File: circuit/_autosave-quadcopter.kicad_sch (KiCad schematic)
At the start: 79 parts, among them J1 Conn_01x01_Female, J10 Conn_01x01_Female, J11 Conn_01x01_Female, J12 Conn_01x01_Female, J13 Conn_01x01_Female, J14 Conn_01x01_Female, J15 Conn_01x01_Female, J16 Conn_01x01_Female, J17 Conn_01x01_Female, J18 USB_C_Receptacle_USB2.0, J19 Conn_01x08_Male, J2 Conn_01x01_Female, J20 Conn_01x04_Male, J21 Conn_01x01_Female, J22 Conn_01x01_Female, J23 Conn_01x01_Female, J24 Conn_01x01_Female, J25 Conn_01x01_Female, J26 Conn_01x01_Female, J27 Conn_01x01_Female, J28 Conn_01x01_Female, J29 Conn_01x01_Female, J3 Conn_01x01_Female, J30 Conn_01x01_Female, J31 Conn_01x01_Female, J32 Conn_01x01_Female, J33 Conn_01x01_Female, J36 Conn_01x01_Female, J37 Conn_01x01_Female, J38 Conn_01x01_Female, J39 Conn_01x01_Female, J4 Conn_01x01_Female, J40 Conn_01x01_Female, J41 Conn_01x01_Female, J42 Conn_01x01_Female, J43 Conn_01x01_Female, J44 Conn_01x01_Female, J45 Conn_01x01_Female, J46 Conn_01x01_Female, J47 Conn_01x01_Female, J48 Conn_01x01_Female, J49 Conn_01x01_Female, J5 Conn_01x01_Female, J50 Conn_01x01_Female, J6 Conn_01x01_Female, J7 Conn_01x01_Female, J8 Conn_01x01_Female, J9 Conn_01x01_Female, SW1 SW_Push_Dual, U1 STM32G431CBU6, U2 ICM-42605, U3 DPS310, U4 3V3, U5 5V, Y1 16M

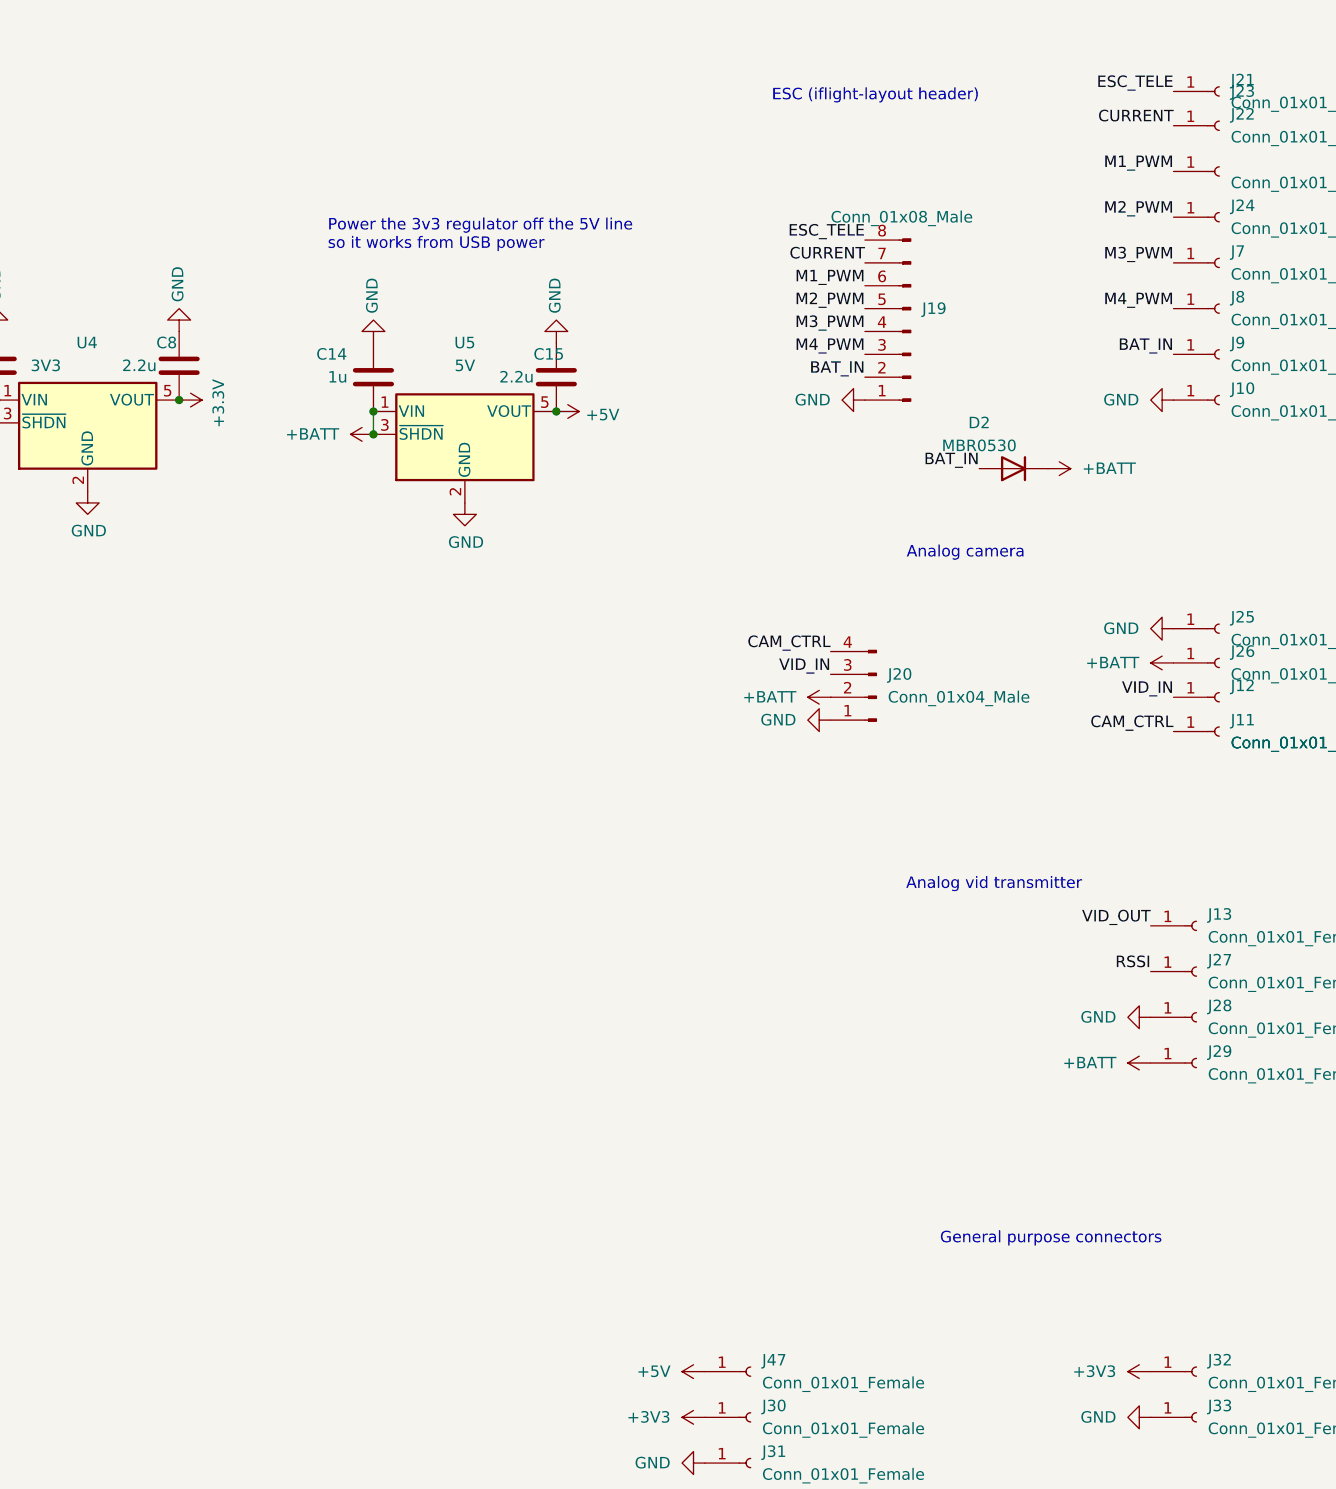
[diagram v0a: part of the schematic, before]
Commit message: Attempting to make the board compatible with 20mm frames
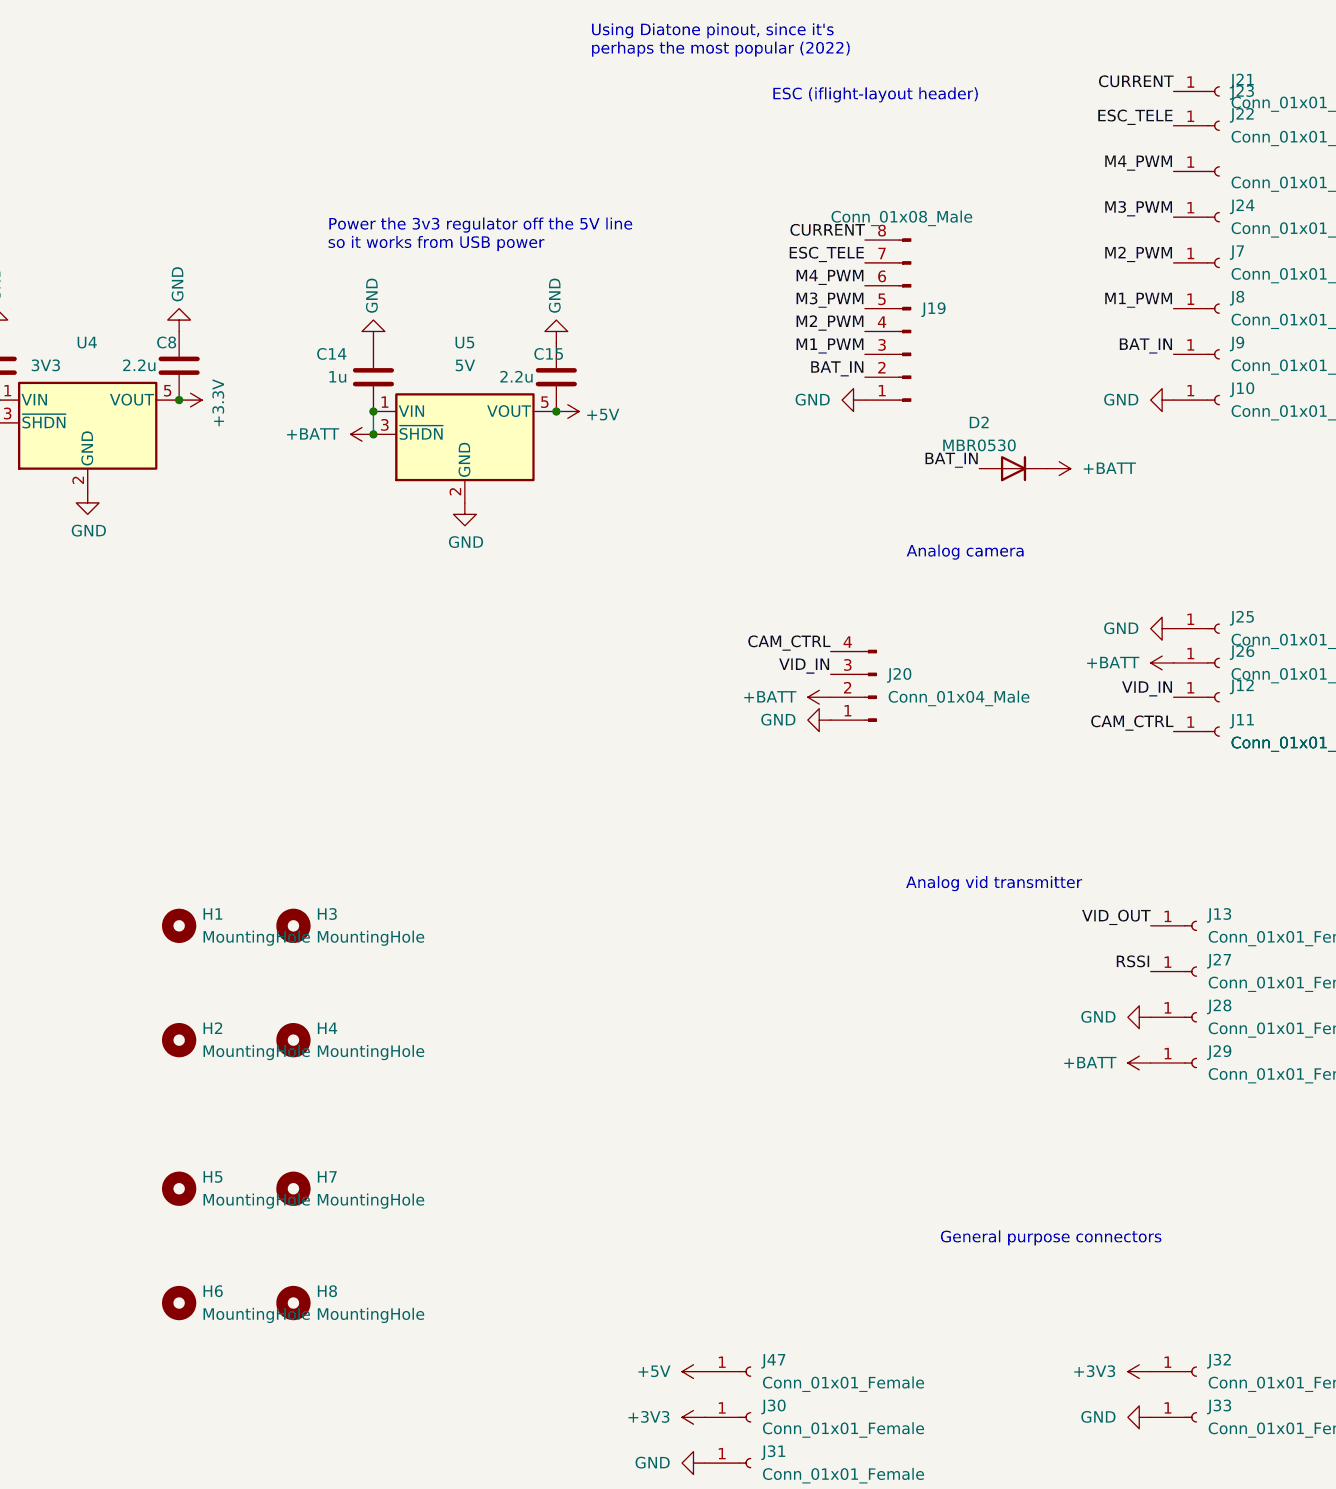
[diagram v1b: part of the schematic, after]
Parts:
- added H1, H2, H3, H4: MountingHole, MountingHole:MountingHole_3.2mm_M3, symbol Mechanical:MountingHole
- added H5, H6, H7, H8: MountingHole, MountingHole:MountingHole_2.2mm_M2, symbol Mechanical:MountingHole
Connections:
- net CURRENT: now also J19.8 (Pin_8), J21.1 (Pin_1); no longer J19.7 (Pin_7), J22.1 (Pin_1)
- net ESC_TELE: now also J19.7 (Pin_7), J22.1 (Pin_1); no longer J19.8 (Pin_8), J21.1 (Pin_1)
- net M1_PWM: now also J19.3 (Pin_3), J8.1 (Pin_1); no longer J19.6 (Pin_6), J23.1 (Pin_1)
- net M2_PWM: now also J19.4 (Pin_4), J7.1 (Pin_1); no longer J19.5 (Pin_5), J24.1 (Pin_1)
- net M3_PWM: now also J19.5 (Pin_5), J24.1 (Pin_1); no longer J19.4 (Pin_4), J7.1 (Pin_1)
- net M4_PWM: now also J19.6 (Pin_6), J23.1 (Pin_1); no longer J19.3 (Pin_3), J8.1 (Pin_1)
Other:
- note added: "Using Diatone pinout, since it's perhaps the most popular (2022)"

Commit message: More work on PCB
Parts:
- added C16, C17: 100n, Capacitor_SMD:C_0402_1005Metric, symbol Device:C
- H5, H6, H7, H8: footprint MountingHole:MountingHole_2.2mm_M2 -> MountingHole:MountingHole_3.2mm_M3
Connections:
- net +3V3: now also C10.2, C11.2, C12.2, C13.2, U1.1 (VBAT), U1.20 (VREF+), U1.21 (VDDA), U1.23 (VDD), U1.35 (VDD), U1.48 (VDD), C16.2, C17.2
- net GND: now also C10.1, C11.1, C12.1, C13.1, U1.49 (EP-GND), C16.1, C17.1
- net at U1.5 (PF0-OSC_IN): now also C6.2, Y1.1
- net at U1.6 (PF1-OSC_OUT): now also C9.2, Y1.3
- now unconnected: U1.8 (PF0-OSC_IN), U1.9 (PF1-OSC_OUT)
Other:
- moved on the sheet: C10, C11, C12, C13

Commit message: More work on PCB
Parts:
- removed SW1: SW_Push_Dual, Button_Switch_THT:SW_PUSH_6mm_H9.5mm, symbol Switch:SW_Push_Dual
- added SW1: SW_DIP_x01, Anyleaf_Shared:SW-SMD-2_3.6x6.0x8.0, symbol Switch:SW_DIP_x01
- J11, J12, J25, J26: footprint TestPoint:TestPoint_Pad_2.0x2.0mm -> TestPoint:TestPoint_Pad_1.5x1.5mm
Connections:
- net SCK_I2C_2 is gone; now on net SCL2: U3.4 (SCK)
- net SDA_2 is gone; now on net SDA2: U3.3 (SDI)
- net +3V3: now also R6.2; no longer R6.1
- net BOOT0: now also R1.2, U1.46 (PB8-BOOT0), SW1.1
- net GND: now also R1.1; no longer R1.2
- net SCL1: now also J15.1 (Pin_1); no longer J5.1 (Pin_1)
- net SCL3: now also J5.1 (Pin_1); no longer J15.1 (Pin_1)
- net SDA1: now also J46.1 (Pin_1); no longer J6.1 (Pin_1)
- net SDA3: now also J6.1 (Pin_1); no longer J46.1 (Pin_1)
- net UART1_RX: now also J45.1 (Pin_1); no longer J37.1 (Pin_1)
- net UART1_TX: now also J44.1 (Pin_1); no longer J36.1 (Pin_1)
- net UART2_RX: now also J43.1 (Pin_1); no longer J39.1 (Pin_1)
- net UART2_TX: now also J42.1 (Pin_1); no longer J38.1 (Pin_1)
- net UART4_RX: now also J39.1 (Pin_1); no longer J43.1 (Pin_1)
- net UART4_TX: now also J38.1 (Pin_1); no longer J42.1 (Pin_1)
- net UART5_RX: now also J37.1 (Pin_1); no longer J45.1 (Pin_1)
- net UART5_TX: now also J36.1 (Pin_1); no longer J44.1 (Pin_1)
- new net: R6.1, SW1.2
- no-connect marks 2 -> 1
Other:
- moved on the sheet: J30, J48, R1, R6

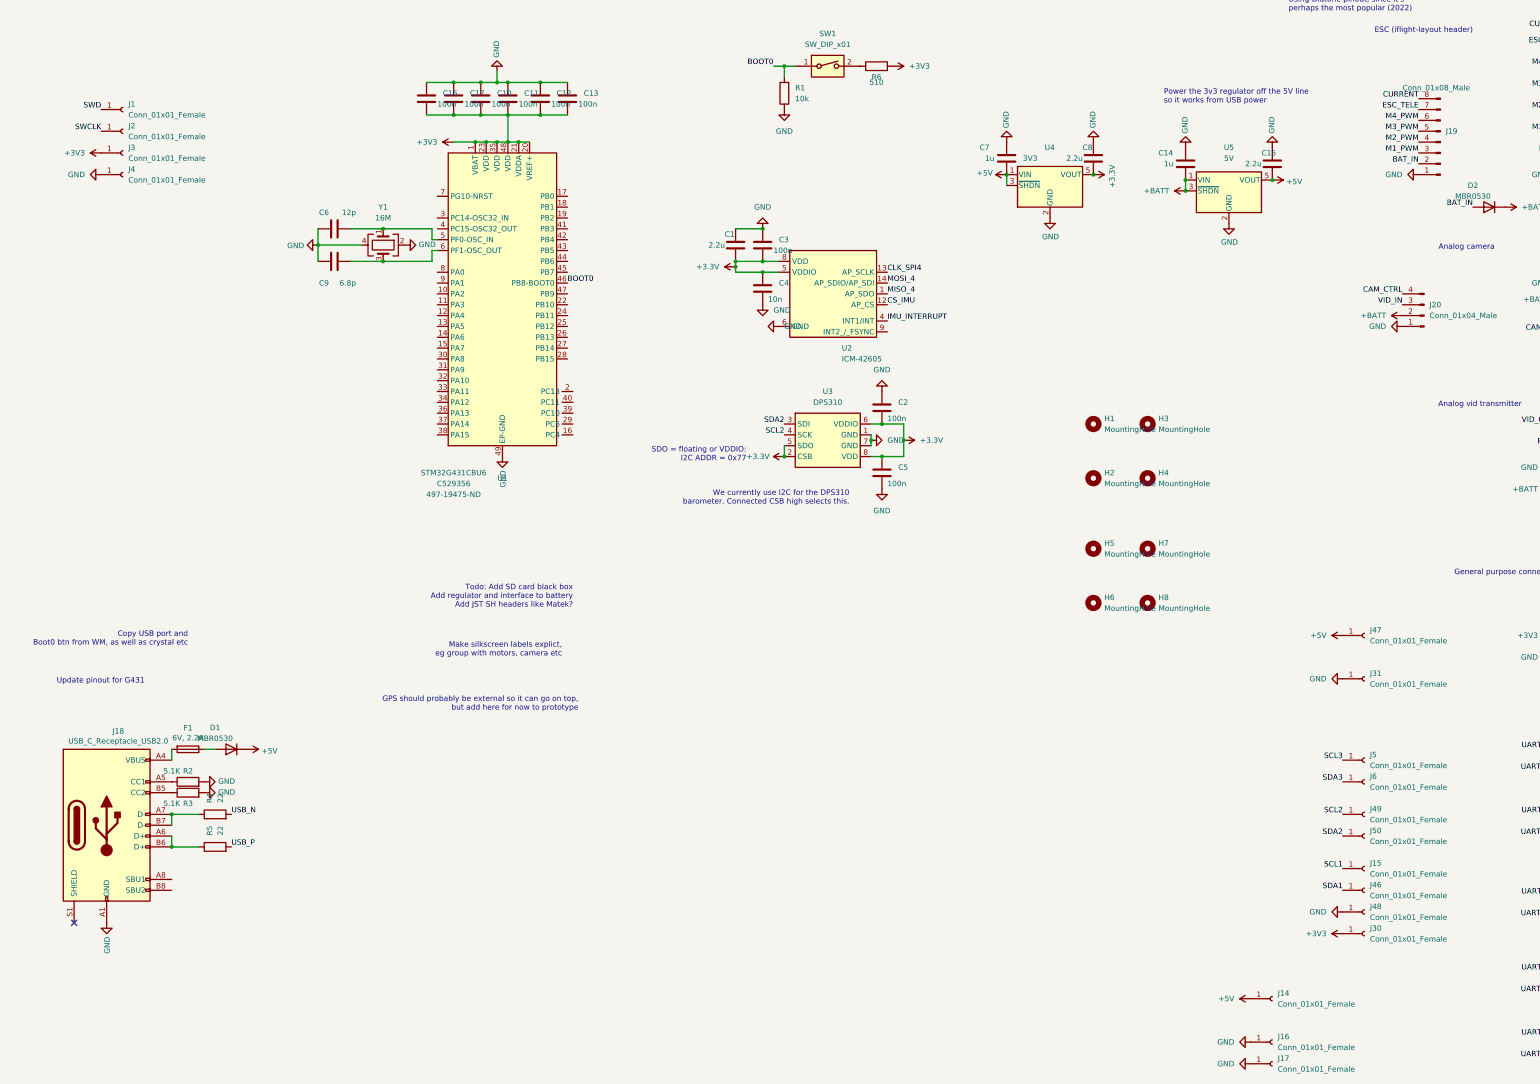
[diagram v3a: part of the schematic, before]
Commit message: More work on PCB, including adding OSD, flash, more labels, exposed pad tweaking
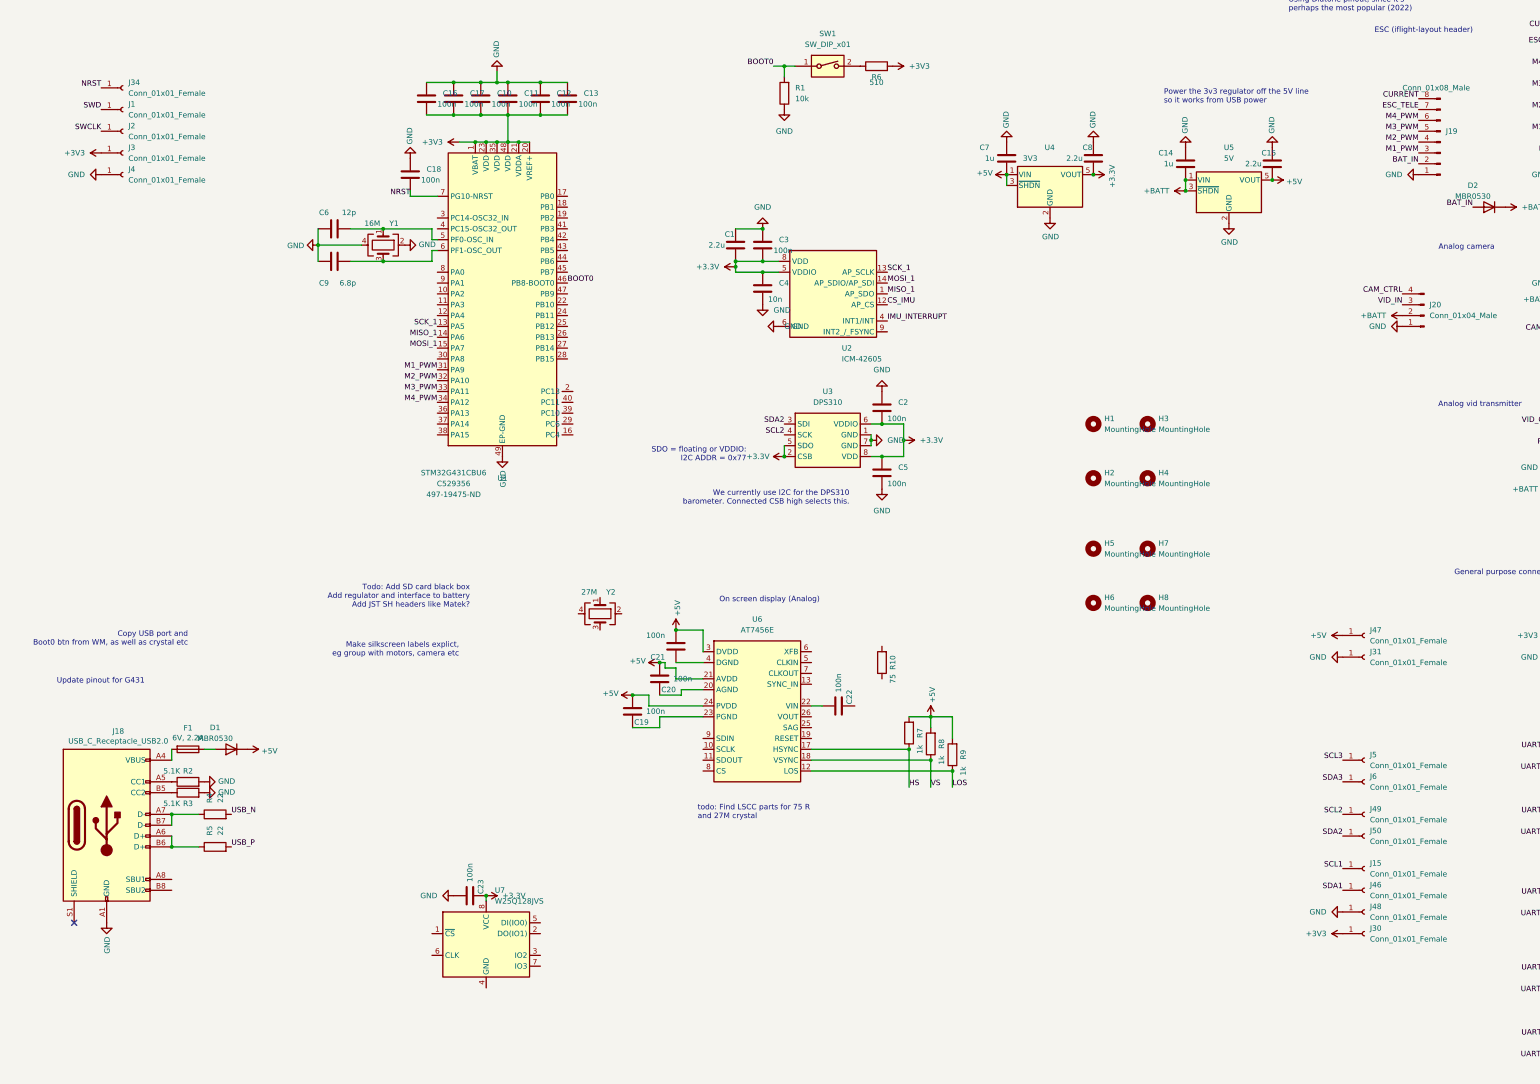
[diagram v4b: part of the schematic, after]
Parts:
- removed J14, J16, J17: Conn_01x01_Female, TestPoint:TestPoint_Pad_2.0x2.0mm, symbol Connector:Conn_01x01_Female
- added C18, C19, C20, C21, C22, C23: 100n, Capacitor_SMD:C_0402_1005Metric, symbol Device:C
- added J34: Conn_01x01_Female, TestPoint:TestPoint_Pad_1.0x1.0mm, symbol Connector:Conn_01x01_Female
- added R10: 75, Resistor_SMD:R_0402_1005Metric, symbol Device:R
- added R7, R8, R9: 1k, Resistor_SMD:R_0402_1005Metric, symbol Device:R
- added U6: AT7456E, Package_SO:TSSOP-28_4.4x9.7mm_P0.65mm, symbol Anyleaf_Shared:AT7456E
- added U7: W25Q128JVS, Package_SON:WSON-8-1EP_6x5mm_P1.27mm_EP3.4x4mm, symbol Memory_Flash:W25Q128JVS
- added Y2: 27M, Oscillator:Oscillator_SMD_EuroQuartz_XO32-4Pin_3.2x2.5mm, symbol Device:Crystal_GND24
- J1, J2, J3, J4: footprint TestPoint:TestPoint_Pad_2.0x2.0mm -> TestPoint:TestPoint_Pad_1.0x1.0mm
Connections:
- net CLK_SPI4 is gone; now on net SCK_1: U2.13 (AP_SCLK)
- net MISO_4 is gone; now on net MISO_1: U2.1 (AP_SDO)
- net MOSI_4 is gone; now on net MOSI_1: U2.14 (AP_SDIO/AP_SDI)
- net +3V3: now also C23.1, U7.8 (VCC)
- net +5V: now also C19.2, C20.2, C21.2, R7.2, R8.2, R9.2, U6.21 (AVDD), U6.24 (PVDD), U6.3 (DVDD)
- net GND: now also C18.1, C23.2
- net M1_PWM: now also U1.31 (PA9)
- net M2_PWM: now also U1.32 (PA10)
- net M3_PWM: now also U1.33 (PA11)
- net M4_PWM: now also U1.34 (PA12)
- net SCK_1: now reaches U1.13 (PA5)
- net MISO_1: now reaches U1.14 (PA6)
- net MOSI_1: now reaches U1.15 (PA7)
- net NRST: now reaches U1.7 (PG10-NRST)
- net NRST: now also C18.2, J34.1 (Pin_1)
- new net: C20.1, U6.20 (AGND)
- new net: C19.1, U6.23 (PGND)
- new net: C22.2, U6.22 (VIN)
- new net: C21.1, U6.4 (DGND)
- new net HS: R7.1, U6.17 (HSYNC)
- new net LOS: R9.1, U6.12 (LOS)
- new net VS: R8.1, U6.18 (VSYNC)
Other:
- note added: "On screen display (Analog)"
- note added: "todo: Find LSCC parts for 75 R and 27M crystal"
- note removed: "GPS should probably be external so it can go on top, but add here for now to prototype"
- moved on the sheet: J31
